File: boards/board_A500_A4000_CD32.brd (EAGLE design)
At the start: 22.5 x 54.6 mm, 3 parts

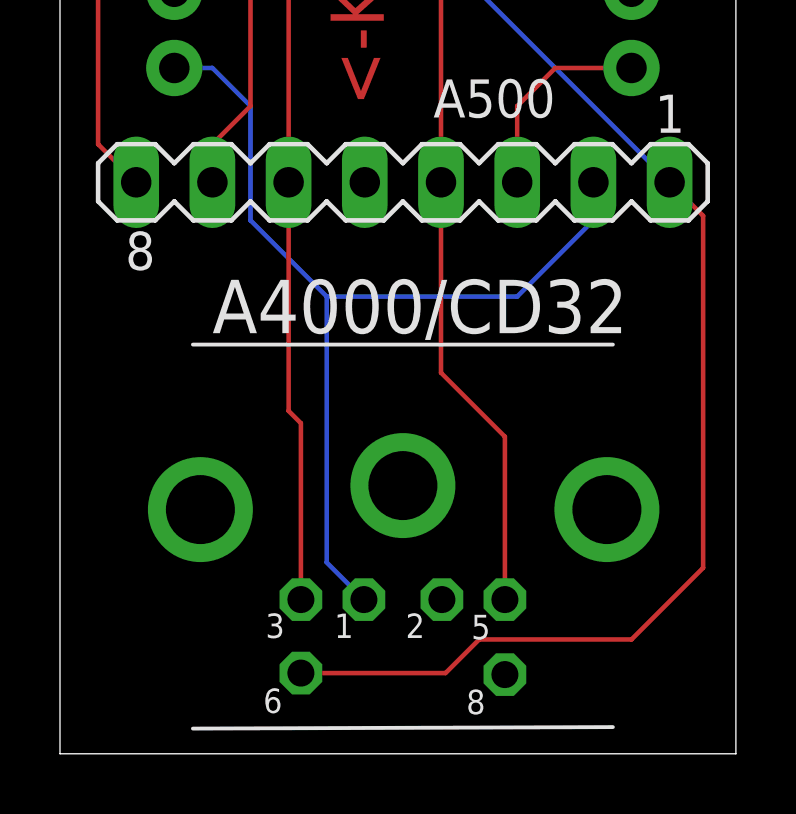
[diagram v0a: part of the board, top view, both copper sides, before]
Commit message: fix socket orientation
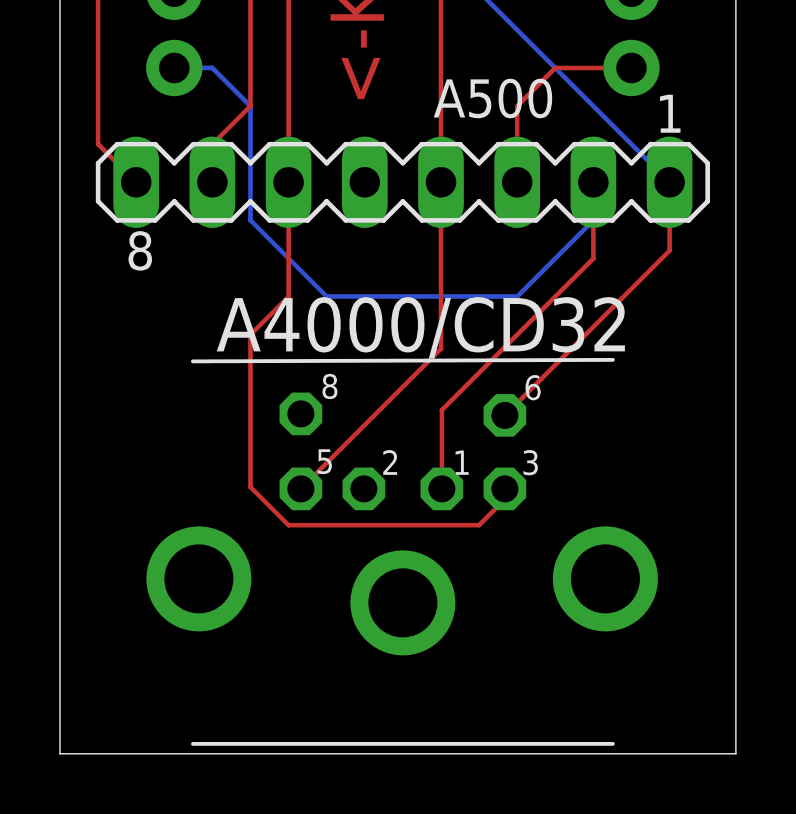
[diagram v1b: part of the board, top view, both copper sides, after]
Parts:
- moved A4000/CD32 3.81 mm to (14.0, 30.5), turned to 180 degrees
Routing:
- net KBCLK: track 47.3 -> 29.2 mm
- net GND: track 58.6 -> 64.9 mm
- net VCC: track 43.8 -> 41.1 mm
- net KBDATA: track 32.3 -> 34.0 mm
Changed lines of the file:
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@@
 <attribute name="VALUE" x="15.24" y="47.371" size="1.27" layer="27" ratio="10" rot="R180"/>
 </element>
-<element name="A4000/CD32" library="mini_din" package="M_DIN6" value="" x="13.97" y="34.29" smashed="yes">
-<attribute name="NAME" x="7.62" y="39.42" size="1.778" layer="25" ratio="10"/>
-<attribute name="VALUE" x="7.62" y="36.88" size="1.778" layer="27" ratio="10"/>
+<element name="A4000/CD32" library="mini_din" package="M_DIN6" value="" x="13.97" y="30.48" smashed="yes" rot="R180">
+<attribute name="NAME" x="21.59" y="40.59" size="1.778" layer="25" ratio="10" rot="R180"/>
+<attribute name="VALUE" x="20.32" y="27.89" size="1.778" layer="27" ratio="10" rot="R180"/>
 </element>
 </elements>
@@
 <wire x1="10.16" y1="64.77" x2="10.16" y2="44.45" width="0.1524" layer="1"/>
 <contactref element="A4000/CD32" pad="3"/>
-<wire x1="10.16" y1="36.83" x2="10.16" y2="44.45" width="0.1524" layer="1"/>
-<wire x1="10.57" y1="30.54" x2="10.57" y2="36.42" width="0.1524" layer="1"/>
-<wire x1="10.57" y1="36.42" x2="10.16" y2="36.83" width="0.1524" layer="1"/>
+<wire x1="10.16" y1="44.45" x2="10.16" y2="40.64" width="0.1524" layer="1"/>
+<wire x1="10.16" y1="40.64" x2="8.89" y2="39.37" width="0.1524" layer="1"/>
+<wire x1="8.89" y1="39.37" x2="8.89" y2="34.29" width="0.1524" layer="1"/>
+<wire x1="8.89" y1="34.29" x2="10.16" y2="33.02" width="0.1524" layer="1"/>
+<wire x1="10.16" y1="33.02" x2="16.51" y2="33.02" width="0.1524" layer="1"/>
+<wire x1="16.51" y1="33.02" x2="17.37" y2="33.88" width="0.1524" layer="1"/>
+<wire x1="17.37" y1="33.88" x2="17.37" y2="34.23" width="0.1524" layer="1"/>
 </signal>
 <signal name="KBCLK">
@@
 <wire x1="16.51" y1="50.8" x2="22.86" y2="44.45" width="0.1524" layer="16"/>
 <contactref element="A4000/CD32" pad="6"/>
-<wire x1="10.57" y1="28.09" x2="15.39" y2="28.09" width="0.1524" layer="1"/>
-<wire x1="16.51" y1="29.21" x2="15.39" y2="28.09" width="0.1524" layer="1"/>
-<wire x1="22.86" y1="44.45" x2="23.9778" y2="43.3322" width="0.1524" layer="1"/>
-<wire x1="23.9778" y1="31.5978" x2="21.59" y2="29.21" width="0.1524" layer="1"/>
-<wire x1="23.9778" y1="43.3322" x2="23.9778" y2="31.5978" width="0.1524" layer="1"/>
-<wire x1="21.59" y1="29.21" x2="16.51" y2="29.21" width="0.1524" layer="1"/>
+<wire x1="17.37" y1="36.68" x2="22.86" y2="42.17" width="0.1524" layer="1"/>
+<wire x1="22.86" y1="42.17" x2="22.86" y2="44.45" width="0.1524" layer="1"/>
 </signal>
 <signal name="KBDATA">
@@
 <wire x1="17.78" y1="40.64" x2="20.32" y2="43.18" width="0.1524" layer="16"/>
 <wire x1="20.32" y1="43.18" x2="20.32" y2="44.45" width="0.1524" layer="16"/>
-<wire x1="11.43" y1="31.78" x2="12.67" y2="30.54" width="0.1524" layer="16"/>
-<wire x1="11.43" y1="40.64" x2="11.43" y2="31.78" width="0.1524" layer="16"/>
+<wire x1="15.27" y1="34.23" x2="15.27" y2="36.86" width="0.1524" layer="1"/>
+<wire x1="15.27" y1="36.86" x2="20.32" y2="41.91" width="0.1524" layer="1"/>
+<wire x1="20.32" y1="41.91" x2="20.32" y2="44.45" width="0.1524" layer="1"/>
 </signal>
 <signal name="VCC">
@@
 <wire x1="17.78" y1="68.58" x2="21.59" y2="68.58" width="0.1524" layer="1"/>
 <contactref element="A4000/CD32" pad="5"/>
-<wire x1="15.24" y1="44.45" x2="15.24" y2="38.1" width="0.1524" layer="1"/>
-<wire x1="17.37" y1="35.97" x2="17.37" y2="30.54" width="0.1524" layer="1"/>
-<wire x1="15.24" y1="38.1" x2="17.37" y2="35.97" width="0.1524" layer="1"/>
+<wire x1="10.57" y1="34.23" x2="15.24" y2="38.9" width="0.1524" layer="1"/>
+<wire x1="15.24" y1="38.9" x2="15.24" y2="44.45" width="0.1524" layer="1"/>
 </signal>
 <signal name="STATUS">
